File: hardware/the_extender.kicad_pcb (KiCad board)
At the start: 4 copper layers, 118 parts, among them J0 U262-241N-4BV60, J1 USB_C_Receptacle_USB2.0, J2 U231-091N-3BLRC11, J3 PJ-3136-B, J4 PJ-3136-B, J5 AF 10.0 HC6.3, J6 Conn_01x03_Female, Q1 SSM3J332R,LF, Q2 SSM3J332R,LF, Q3 Q_PNP_CBE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

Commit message: done some more stuff
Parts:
- moved Q4 0.36 mm to (81.8, 34.5)
- moved C33 0.25 mm to (92.5, 40.1)
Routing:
- net Net-(R26-Pad2): track 1.75 -> 22.3 mm
- net Net-(U2-Pad55): track 0.00 -> 18.9 mm
- net Net-(U2-Pad54): track 0.00 -> 16.7 mm
- net Net-(U2-Pad51): track 0.00 -> 14.8 mm
- net Net-(U2-Pad52): track 0.00 -> 12.3 mm
- net +1V1: track 2.24 -> 13.5 mm
- net Net-(U2-Pad53): track 0.00 -> 10.2 mm
- net +3V3: track 53.1 -> 57.9 mm, vias 9 -> 8
- net unconnected-(U6-Pad39): track 0.00 -> 3.26 mm
- net Net-(C9-Pad1): track 3.26 -> 0.00 mm
- net CLK_24M: track 1.91 -> 4.55 mm, vias 1 -> 2
- net SCL: track 3.74 -> 5.97 mm, vias 2 -> 3
- net GND: track 110.5 -> 108.9 mm, vias 36 -> 37
- net HUB_EN: track 0.00 -> 1.47 mm, vias 0 -> 1
- net SDA: track 3.58 -> 4.54 mm, vias 2 -> 3
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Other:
- board outline added: 51.1 x 50.6 mm

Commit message: i might have finished routing signals
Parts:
- TP1, TP10, TP11, TP12, TP13, TP14, TP2, TP3, TP4, TP5, TP6, TP7, TP8, TP9: moved to F.Cu
- moved TP8 130.3 mm to (139.5, 67.8), turned to 0 degrees
- moved TP7 123.5 mm to (143.5, 59.7), turned to 0 degrees
- moved TP3 117.4 mm to (147.6, 59.7), turned to 0 degrees
- moved TP13 108.7 mm to (139.5, 63.8), turned to 0 degrees
- moved TP1 108.1 mm to (147.6, 63.8), turned to 0 degrees
- moved TP2 98.9 mm to (151.6, 59.7), turned to 0 degrees
- moved TP5 91.2 mm to (151.6, 63.8), turned to 0 degrees
- moved TP10 88.5 mm to (143.5, 67.8), turned to 0 degrees
- moved TP14 88.5 mm to (147.6, 67.8), turned to 0 degrees
- moved C38 83.7 mm to (73.9, 44.5), turned to 180 degrees
- moved TP9 78.9 mm to (139.5, 59.7), turned to 0 degrees
- moved C40 77.8 mm to (65.9, 47.6)
- moved TP4 75.7 mm to (155.7, 63.8), turned to 0 degrees
- moved C34 74.8 mm to (81.0, 36.3)
- moved TP12 73.8 mm to (155.7, 59.7), turned to 0 degrees
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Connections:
- net RP_LED renamed MCU_LED
- U2 pad 15: HUB_SCL -> unconnected-(U2-Pad15)
- U2 pad 16: HUB_SDA -> unconnected-(U2-Pad16)
- U2 pad 17: SND_EEPROM_DR -> CC_USB_INT
- U2 pad 18: SND_EEPROM_DW -> unconnected-(U2-Pad18)
- U2 pad 27: SND_EEPROM_SCK -> unconnected-(U2-Pad27)
- U2 pad 28: SND_EEPROM_CS -> unconnected-(U2-Pad28)
- U2 pad 29: unconnected-(U2-Pad29) -> SND_EEPROM_DR
- U2 pad 30: unconnected-(U2-Pad30) -> SND_EEPROM_DW
- U2 pad 31: unconnected-(U2-Pad31) -> SND_EEPROM_SCK
- U2 pad 32: unconnected-(U2-Pad32) -> SND_EEPROM_CS
- U2 pad 35: unconnected-(U2-Pad35) -> HUB_SDA
- U2 pad 36: unconnected-(U2-Pad36) -> HUB_SCL
- U2 pad 38: MIC_T -> MIC_R
- U2 pad 39: MIC_R -> unconnected-(U2-Pad39)
- U2 pad 41: unconnected-(U2-Pad41) -> MIC_T
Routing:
- net +5V: track 63.1 -> 163.9 mm, vias 6 -> 9
- net GND: track 108.9 -> 206.1 mm, vias 37 -> 58
- net USB3RX-: track 0.00 -> 82.5 mm, vias 0 -> 1
- net USB3RX+: track 0.00 -> 80.3 mm
- net USB3TX-: track 0.00 -> 67.6 mm, vias 0 -> 1
- net USB3TX+: track 0.00 -> 66.1 mm, vias 0 -> 1
- net SDA: track 4.54 -> 67.9 mm, vias 3 -> 4
- net SCL: track 5.97 -> 65.0 mm, vias 3 -> 4
- net +BATT: track 74.2 -> 133.3 mm, vias 4 -> 8
- net MIC_T: track 14.1 -> 60.9 mm, vias 0 -> 2
- net CC_USB_INT: track 0.00 -> 44.7 mm, vias 0 -> 2
- net MCU_LED: track 0.00 -> 41.2 mm, vias 0 -> 3
- net +3V3: track 57.9 -> 98.4 mm, vias 8 -> 11
- net +3.3VP: track 23.2 -> 62.0 mm
- net MIC_R: track 29.7 -> 66.9 mm, vias 1 -> 2
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- added copper zone on B.Cu, net GND
- added copper zone on In1.Cu, net GND
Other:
- board size 51.1 x 50.6 mm -> 51.2 x 50.6 mm

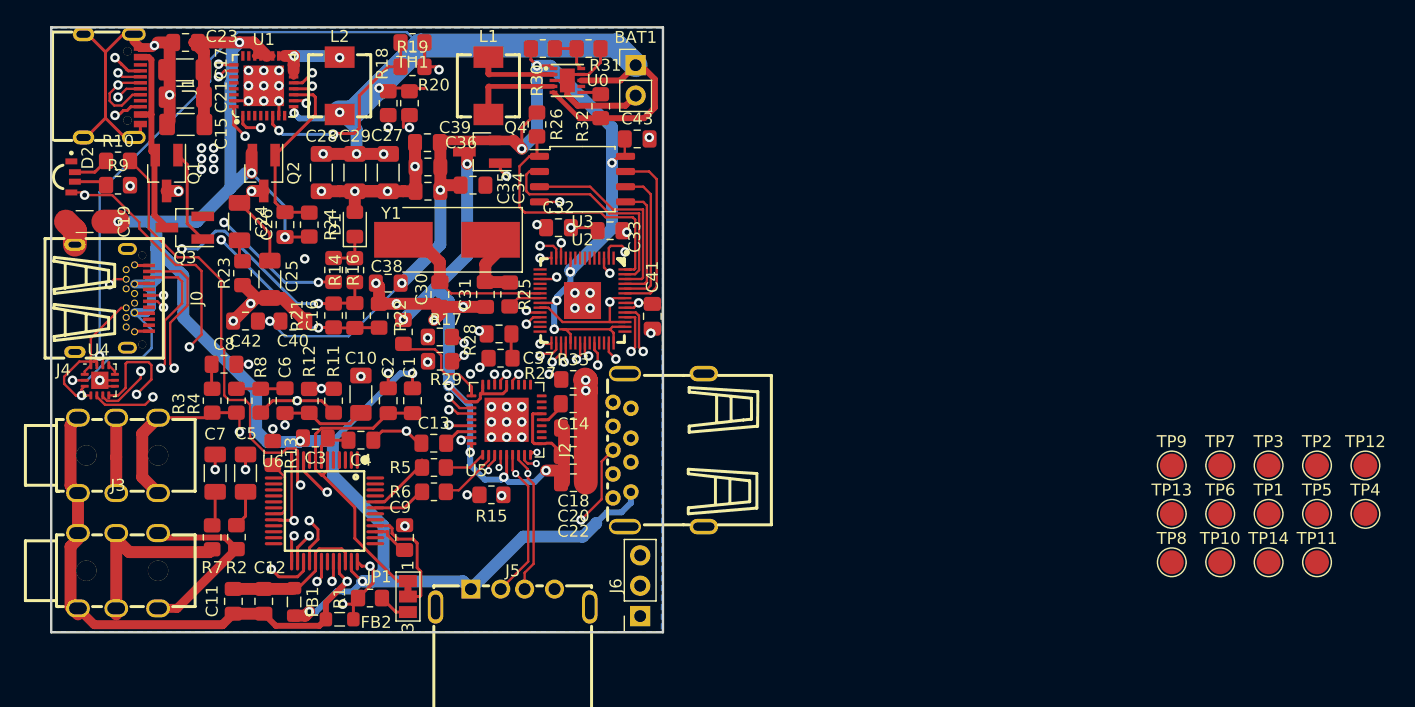
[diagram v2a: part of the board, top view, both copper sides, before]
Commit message: ground planes in
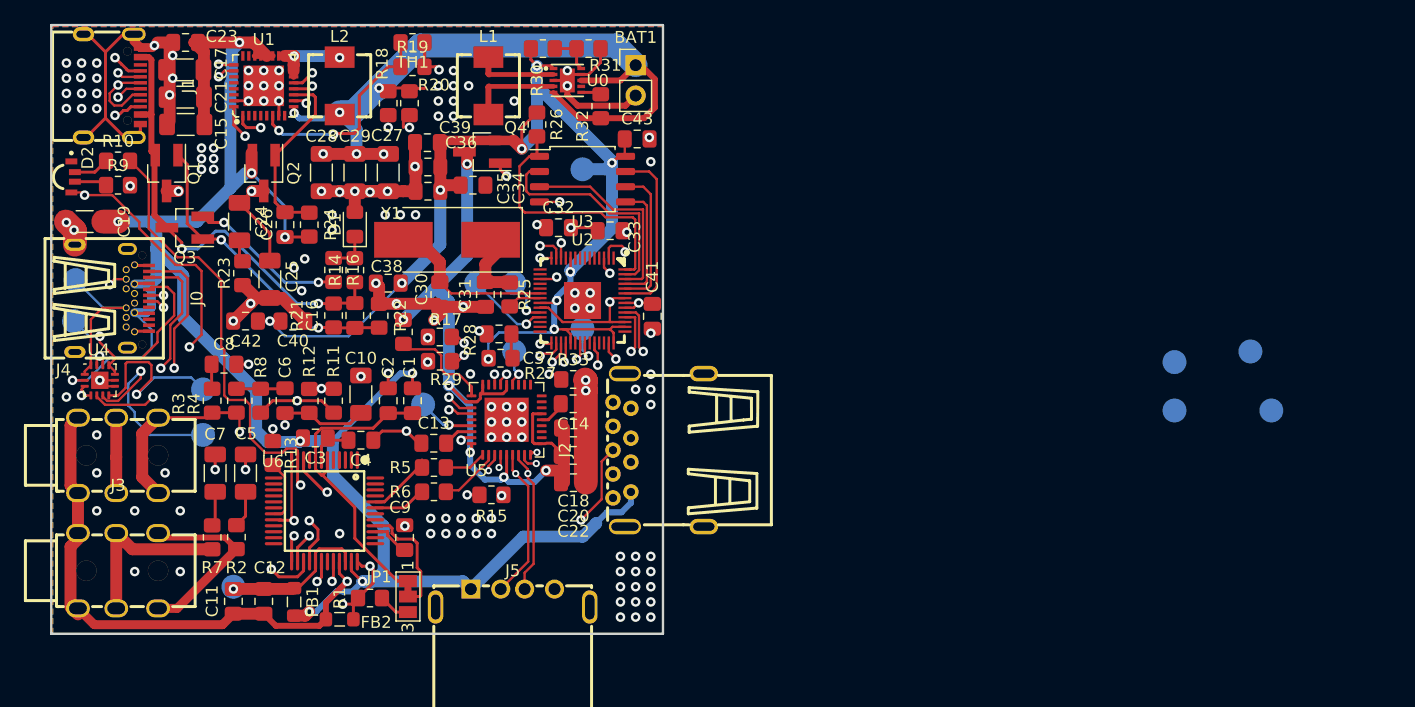
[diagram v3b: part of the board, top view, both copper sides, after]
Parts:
- removed J6: Conn_01x03_Female, Connector_PinSocket_2.54mm:PinSocket_1x03_P2.54mm_Vertical
- added TP15: SWD, TestPoint:TestPoint_Pad_D2.0mm, B.Cu at (81.3, 44.5)
- TP1, TP11, TP12, TP13, TP14, TP2, TP3, TP4, TP5, TP6, TP7, TP8, TP9: moved to B.Cu
- TP10: value ? -> SWCLK; moved to B.Cu
- moved TP4 109.7 mm to (47.8, 44.2), turned to 90 degrees
- moved TP3 100.7 mm to (47.6, 47.6), turned to 90 degrees
- moved TP5 93.8 mm to (58.4, 53.3), turned to 180 degrees
- moved TP2 91.2 mm to (61.0, 69.8), turned to 180 degrees
- moved TP6 85.4 mm to (58.4, 57.1), turned to 180 degrees
- moved TP1 64.2 mm to (90.2, 34.9), turned to 180 degrees
- moved TP10 63.5 mm to (84.5, 44.5), turned to 180 degrees
- moved TP9 62.8 mm to (76.8, 54.6), turned to 180 degrees
- moved TP7 59.8 mm to (84.5, 50.2), turned to 180 degrees
- moved TP8 53.0 mm to (90.2, 48.3), turned to 180 degrees
- moved TP12 18.2 mm to (139.7, 51.1), turned to 180 degrees
- moved TP14 17.7 mm to (146.1, 50.2), turned to 180 degrees
- moved TP11 17.4 mm to (139.7, 55.1), turned to 180 degrees
- moved TP13 12.0 mm to (147.8, 55.1), turned to 180 degrees
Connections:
- C11 pad 1: Net-(C11-Pad1) -> +5VA
- C12 pad 1: Net-(C11-Pad1) -> +5VA
- FB1 pad 1: Net-(C11-Pad1) -> +5VA
- TP10 pad 1: unconnected-(TP10-Pad1) -> Net-(U2-Pad24)
- U2 pad 24: Net-(J6-Pad1) -> Net-(U2-Pad24)
- U6 pad 29: Net-(C11-Pad1) -> +5VA
- U6 pad 34: Net-(C11-Pad1) -> +5VA
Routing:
- net CC1: track 0.97 -> 18.0 mm, vias 0 -> 1
- net Net-(J3-PadR): track 0.00 -> 14.9 mm
- net GNDA: track 86.3 -> 71.4 mm
- net CC2: track 0.00 -> 13.6 mm
- net Net-(C11-Pad1): track 12.6 -> 0.00 mm
- net +5VA: track 0.00 -> 12.6 mm, vias 0 -> 1
- net +BATT: track 133.3 -> 120.9 mm
- net SCL: track 65.0 -> 76.0 mm
- net +3V3: track 98.4 -> 105.1 mm
- net SDA: track 67.9 -> 74.4 mm
- net Net-(U2-Pad25): track 1.39 -> 7.00 mm
- net Net-(U2-Pad24): track 0.00 -> 3.93 mm, vias 0 -> 1
- net CLK_24M: track 36.4 -> 39.3 mm
- net HUB_SCL: track 11.7 -> 14.2 mm
- net CHG_VBUS: track 36.0 -> 38.2 mm
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- added copper zone on F.Cu, net GND
- added copper zone on In2.Cu, net GND
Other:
- board size 51.2 x 50.6 mm -> 51.2 x 50.9 mm

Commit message: added some missing connections
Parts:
- added R34: 4k7, Resistor_SMD:R_0805_2012Metric_Pad1.20x1.40mm_HandSolder, F.Cu at (66.3, 34.9)
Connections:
- U1 pad 2: unconnected-(U1-Pad2) -> PB_INT
- U2 pad 18: unconnected-(U2-Pad18) -> PB_INT
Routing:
- net PB_INT: track 0.00 -> 35.6 mm, vias 0 -> 3
- net CHG_USBC_D+: track 17.1 -> 0.00 mm
- net GND: track 206.1 -> 223.2 mm, vias 134 -> 154
- net +BATT: track 120.9 -> 123.1 mm

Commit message: fix bugs
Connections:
- C9 pad 1: Net-(C9-Pad1) -> Net-(U6-Pad39)
- U6 pad 39: unconnected-(U6-Pad39) -> Net-(U6-Pad39)
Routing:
- net GND: track 223.2 -> 203.3 mm
- net CHG_USBC_D+: track 0.00 -> 17.1 mm
- net SND_1V8: track 0.00 -> 3.88 mm
- net SND_3V3: track 30.0 -> 26.6 mm
- net Net-(C9-Pad1): track 3.26 -> 0.00 mm
- net Net-(U6-Pad39): track 0.00 -> 3.09 mm
- net GNDA: track 71.4 -> 72.1 mm
- net EXT_USB_D-: vias 1 -> 0
- net EXT_USB_D+: vias 1 -> 0

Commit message: fix bugs
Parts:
- moved TP7 0.65 mm to (83.8, 50.0)
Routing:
- net Net-(C37-Pad1): track 2.34 -> 14.7 mm, vias 0 -> 2
- net +3V3: track 105.6 -> 114.1 mm, vias 11 -> 12
- net HUB_EN: track 16.2 -> 12.7 mm
- net +BATT: track 123.1 -> 125.2 mm
- net SDA: track 74.3 -> 75.3 mm
- net MCU_COMP_D+: track 25.9 -> 26.5 mm
- net CHG_VIN: track 0.00 -> 0.50 mm

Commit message: fix bugs
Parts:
- moved TP14 79.8 mm to (66.8, 59.9)
- moved TP13 77.4 mm to (70.9, 63.2)
- moved TP11 67.1 mm to (72.6, 57.9)
- moved TP12 65.4 mm to (74.9, 60.5)
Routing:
- net SND_EEPROM_CS: track 1.64 -> 33.2 mm, vias 1 -> 2
- net SND_EEPROM_SCK: track 1.91 -> 29.8 mm, vias 1 -> 2
- net SND_EEPROM_DR: track 0.99 -> 25.4 mm, vias 1 -> 2
- net SND_EEPROM_DW: track 2.14 -> 25.9 mm, vias 1 -> 2
- net MIC_R: track 66.9 -> 72.9 mm
- net CLK_24M: track 39.3 -> 37.4 mm
- net SND_LED_O: track 36.8 -> 38.1 mm
- net SND_3V3: track 26.6 -> 27.6 mm, vias 0 -> 2
- net +3V3: track 114.1 -> 114.9 mm

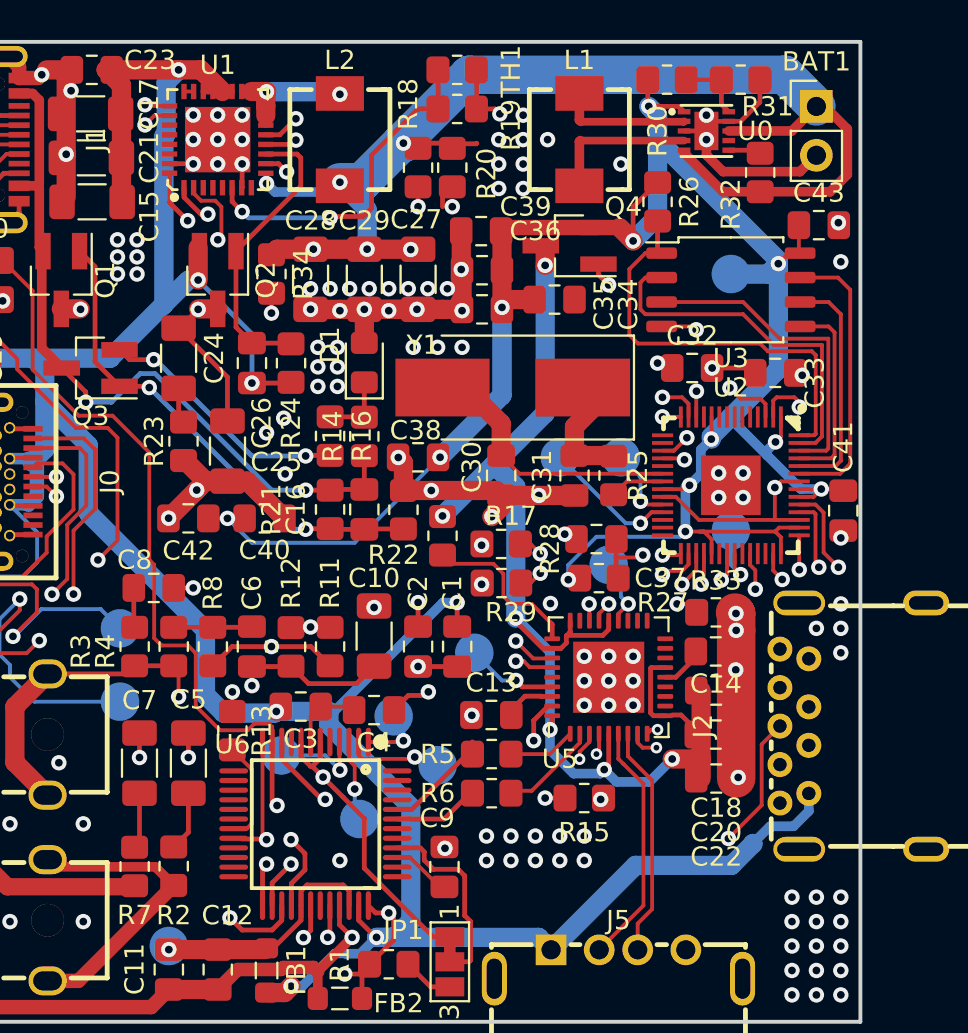
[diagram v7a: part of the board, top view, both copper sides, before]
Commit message: use default footprints
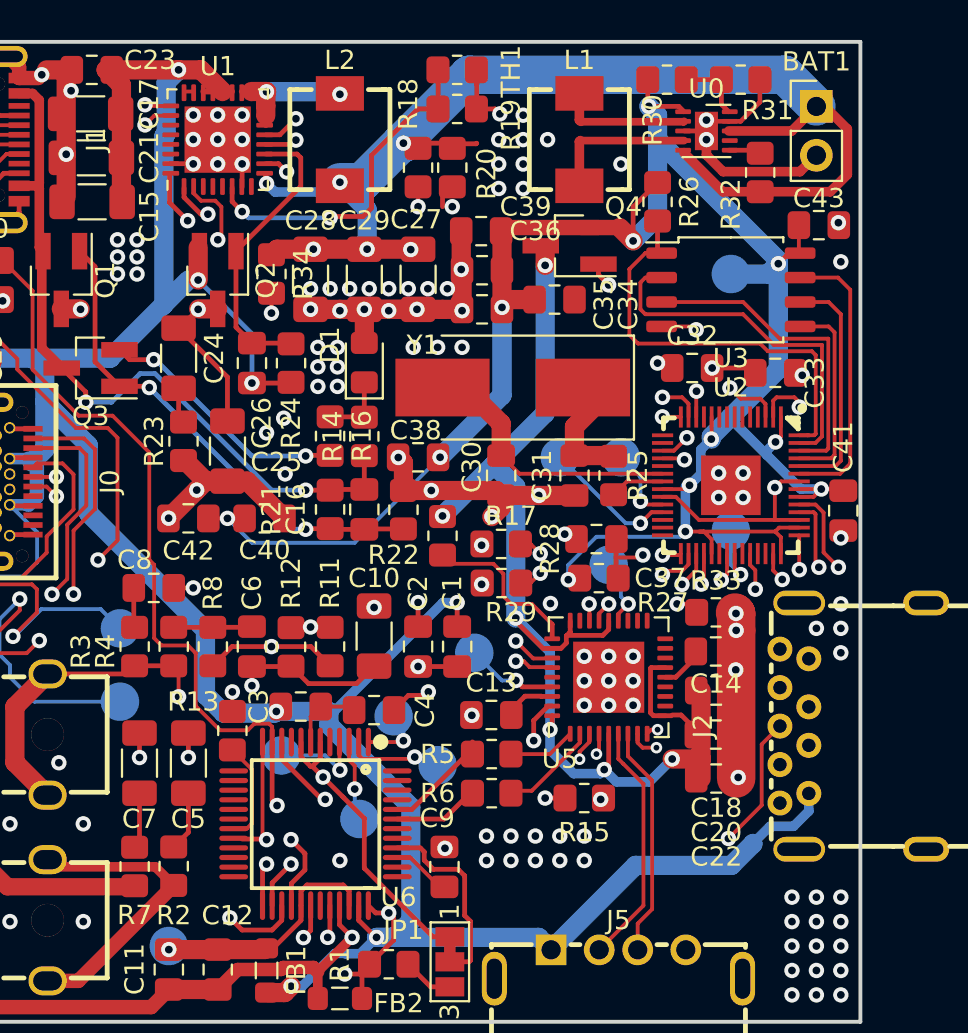
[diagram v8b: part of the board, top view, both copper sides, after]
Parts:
- U0: footprint easyeda2kicad:WSON-10_L2.5-W2.5-P0.50-BL-EP -> Package_SON:WSON-10-1EP_2.5x2.5mm_P0.5mm_EP1.2x2mm
- U1: footprint easyeda2kicad:QFN-32_L5.0-W5.0-P0.50-BL-EP3.4 -> Package_DFN_QFN:QFN-32-1EP_5x5mm_P0.5mm_EP3.45x3.45mm
- turned U0 to 0 degrees
- turned U1 to 90 degrees
